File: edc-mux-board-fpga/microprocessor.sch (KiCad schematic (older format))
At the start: 27 parts

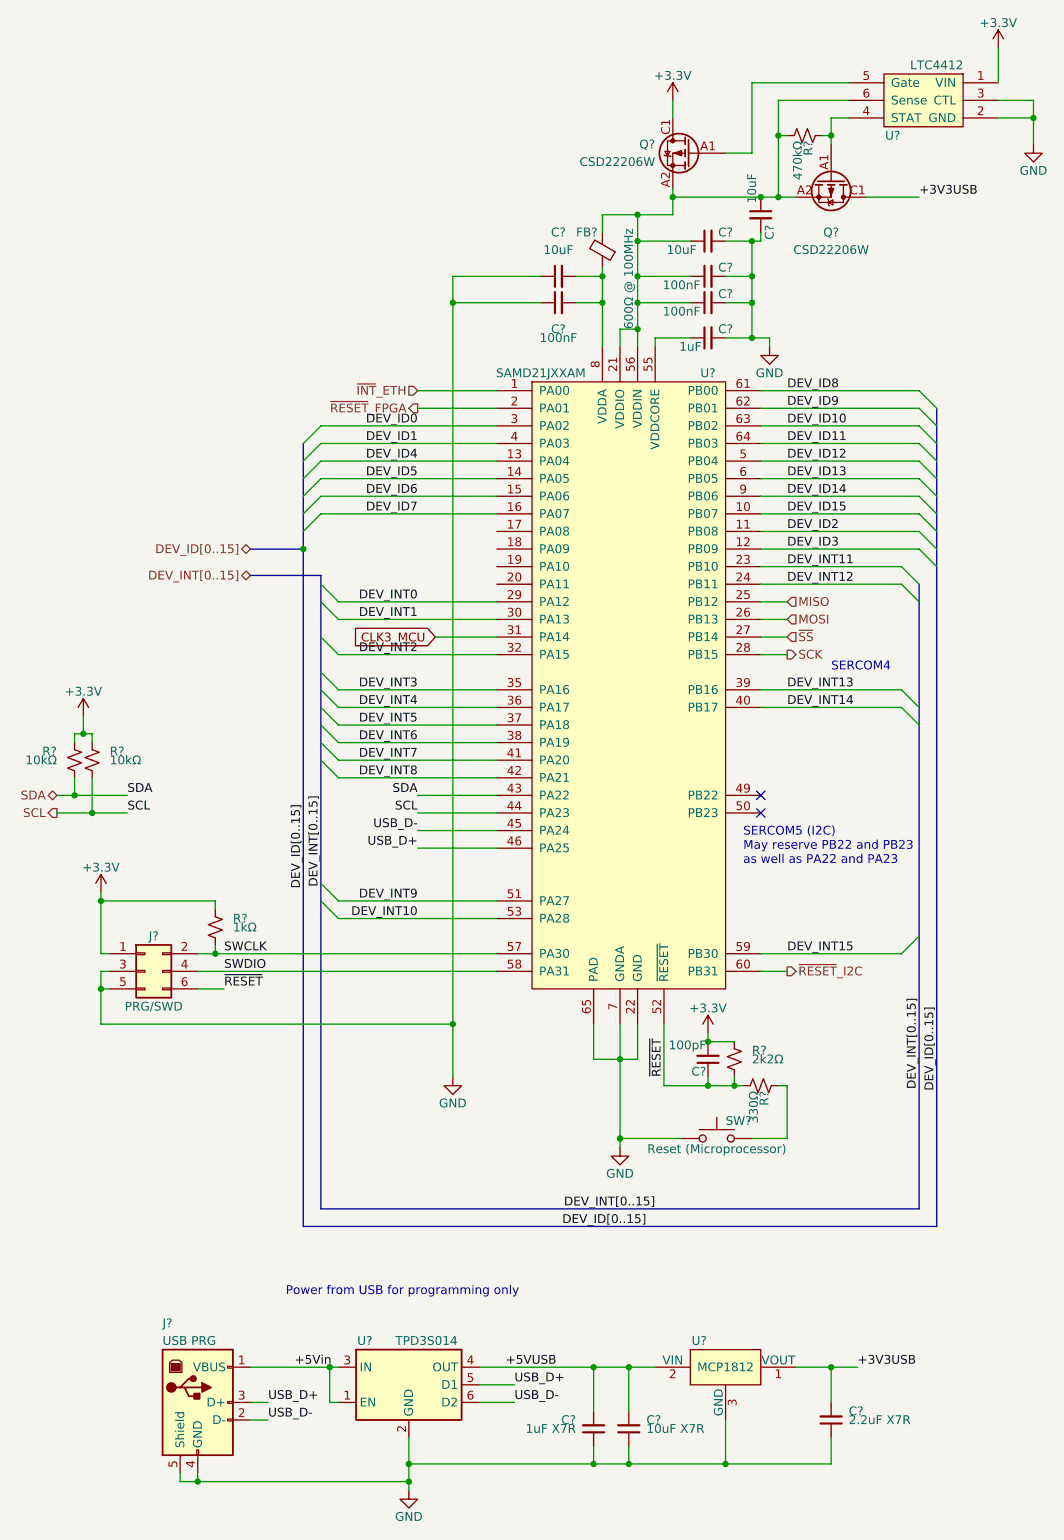
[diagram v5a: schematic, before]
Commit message: Finished FPGA and MCU interconnections.
Finished up interrupt wiring
Fixed a few missing connections
Annotated Schematic
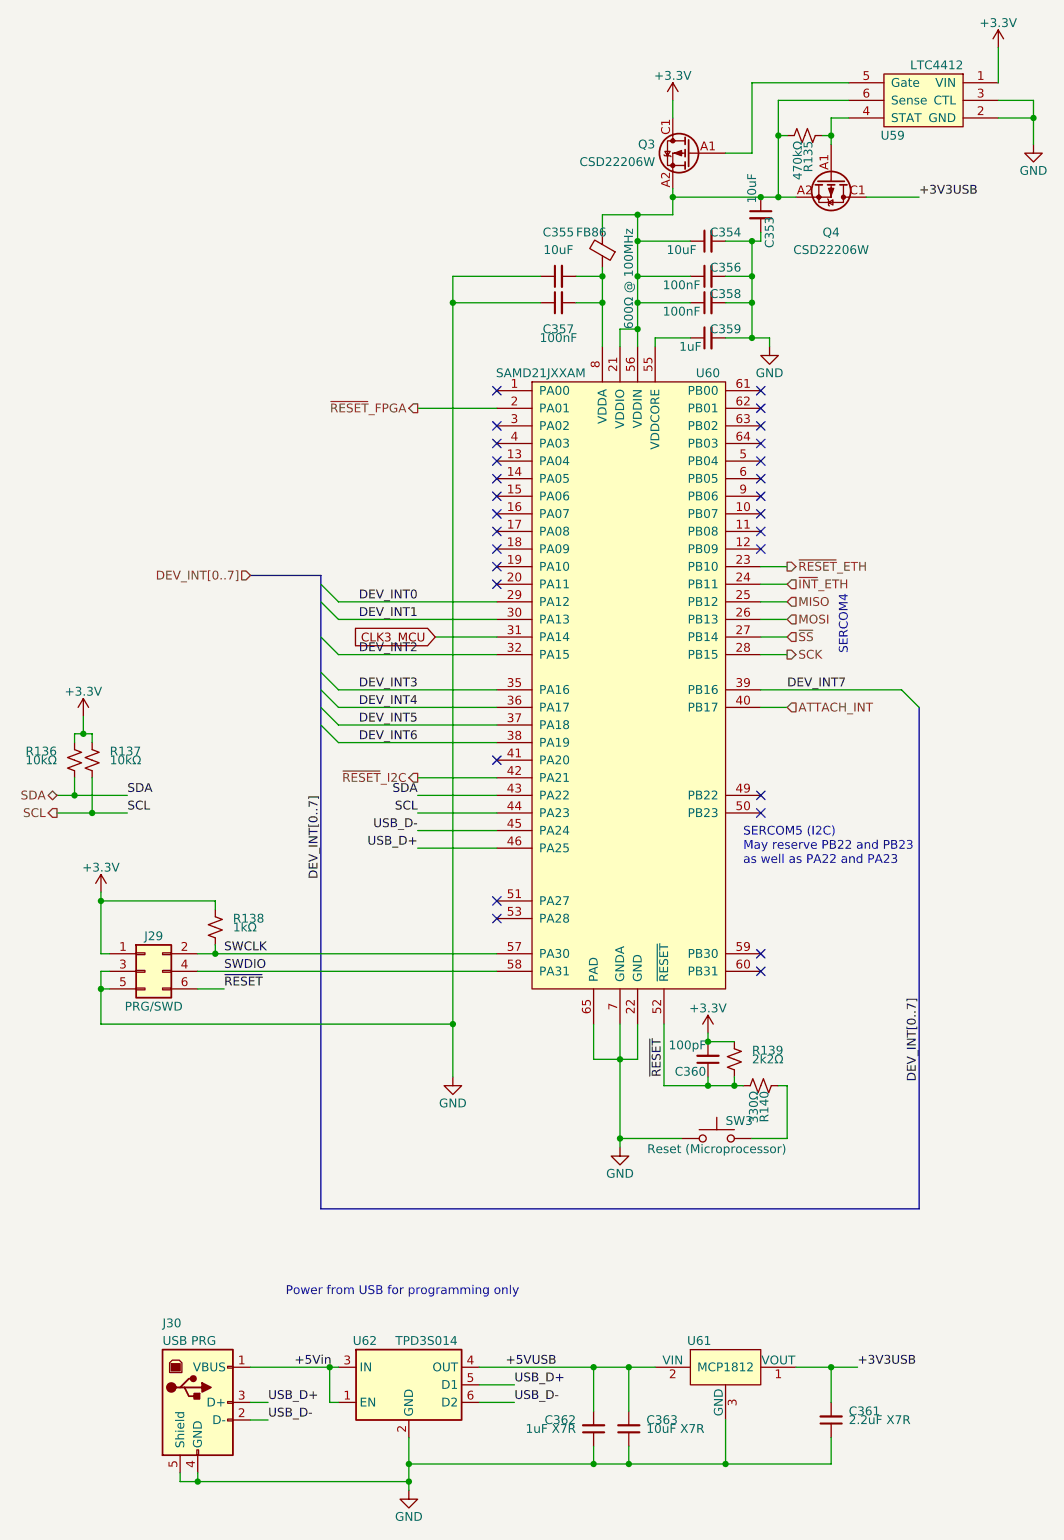
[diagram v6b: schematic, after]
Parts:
- gave numbers to parts that had none: 27
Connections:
- net DEV_INT12 is gone; now on net ~INT~_ETH: U60.24 (PB11)
- net DEV_INT13 is gone; now on net DEV_INT7: U60.39 (PB16)
- net DEV_INT8 is gone; now on net ~RESET~_I2C: U60.42 (PA21)
- net DEV_INT7: no longer U60.41 (PA20)
- net ~INT~_ETH: no longer U60.1 (PA00)
- net ~RESET~_I2C: no longer U60.60 (PB31)
- net DEV_ID0: no longer names the net of U60.3 (PA02)
- net DEV_ID1: no longer names the net of U60.4 (PA03)
- net DEV_ID10: no longer names the net of U60.63 (PB02)
- net DEV_ID11: no longer names the net of U60.64 (PB03)
- net DEV_ID12: no longer names the net of U60.5 (PB04)
- net DEV_ID13: no longer names the net of U60.6 (PB05)
- net DEV_ID14: no longer names the net of U60.9 (PB06)
- net DEV_ID15: no longer names the net of U60.10 (PB07)
- net DEV_ID2: no longer names the net of U60.11 (PB08)
- net DEV_ID3: no longer names the net of U60.12 (PB09)
- net DEV_ID4: no longer names the net of U60.13 (PA04)
- net DEV_ID5: no longer names the net of U60.14 (PA05)
- net DEV_ID6: no longer names the net of U60.15 (PA06)
- net DEV_ID7: no longer names the net of U60.16 (PA07)
- net DEV_ID8: no longer names the net of U60.61 (PB00)
- net DEV_ID9: no longer names the net of U60.62 (PB01)
- net DEV_INT10: no longer names the net of U60.53 (PA28)
- net DEV_INT11 renamed ~RESET~_ETH
- net DEV_INT14 renamed ATTACH_INT
- net DEV_INT15: no longer names the net of U60.59 (PB30)
- net DEV_INT9: no longer names the net of U60.51 (PA27)
- no-connect marks 2 -> 28

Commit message: assigned more footprints
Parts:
- C353, C354, C355: value 10uF -> 10uF X7R; footprint (none) -> Capacitor_SMD:C_1206_3216Metric; Manufacturer (none) -> Kemet; Manufacturers Part Number (none) -> C1206C106J3RACAUTO; Package ID (none) -> 1206in/3216mm
- C356, C357, C358, C360, C361: footprint (none) -> Capacitor_SMD:C_0603_1608Metric; Package ID (none) -> 0603in/1608mm
- C359: value 1uF -> 1uF X7R; footprint (none) -> Capacitor_SMD:C_0603_1608Metric; Manufacturer (none) -> TDK; Manufacturers Part Number (none) -> CGA3E1X7R1E105K080AC; Package ID (none) -> 0603in/1608mm
- C362: footprint (none) -> Capacitor_SMD:C_0603_1608Metric; Manufacturer (none) -> TDK; Manufacturers Part Number (none) -> CGA3E1X7R1E105K080AC; Package ID (none) -> 0603in/1608mm
- C363: footprint (none) -> Capacitor_SMD:C_1206_3216Metric; Manufacturer (none) -> Kemet; Manufacturers Part Number (none) -> C1206C106J3RACAUTO; Package ID (none) -> 1206in/3216mm
- J29: footprint (none) -> Connector_PinHeader_2.54mm:PinHeader_2x03_P2.54mm_Vertical
- J30: footprint (none) -> SW-CUI-INC:UJ2-BV-1-TH
- R135, R136, R137, R138, R139, R140: footprint (none) -> Resistor_SMD:R_0402_1005Metric
- U61: footprint (none) -> Package_TO_SOT_SMD:SOT-23; Description (none) -> 3v3 regulator 300mA; Manufacturer (none) -> Microchip; Manufacturers Part Number (none) -> MCP1812AT-033/TT
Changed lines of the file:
@@
 P 3900 2150
 F 0 "C355" V 4150 2150 50  0000 C CNN
-F 1 "10uF" V 4050 2150 50  0000 C CNN
-F 2 "" H 3900 2150 50  0001 C CNN
+F 1 "10uF X7R" V 4050 2150 50  0000 C CNN
+F 2 "Capacitor_SMD:C_1206_3216Metric" H 3900 2150 50  0001 C CNN
 F 3 "~" H 3900 2150 50  0001 C CNN
+F 4 "Kemet" H 0   0   50  0001 C CNN "Manufacturer"
+F 5 "C1206C106J3RACAUTO" H 0   0   50  0001 C CNN "Manufacturers Part Number"
+F 6 "1206in/3216mm" H 0   0   50  0001 C CNN "Package ID"
 	1    3900 2150
 	0    -1   -1   0
@@
 F 0 "C357" V 3750 2300 50  0000 C CNN
 F 1 "100nF" V 3700 2300 50  0000 C CNN
-F 2 "" H 3900 2300 50  0001 C CNN
+F 2 "Capacitor_SMD:C_0603_1608Metric" H 3900 2300 50  0001 C CNN
 F 3 "~" H 3900 2300 50  0001 C CNN
+F 4 "0603in/1608mm" H 0   0   50  0001 C CNN "Package ID"
 	1    3900 2300
 	0    -1   -1   0
@@
 F 0 "R140" H 5080 6770 50  0000 L CNN
 F 1 "330Ω" H 5080 6710 50  0000 L CNN
-F 2 "" H 5050 6750 50  0001 C CNN
+F 2 "Resistor_SMD:R_0402_1005Metric" H 5050 6750 50  0001 C CNN
 F 3 "~" H 5050 6750 50  0001 C CNN
 	1    5050 6750
@@
 F 0 "C360" H 4760 6670 50  0000 L CNN
 F 1 "100pF" H 4760 6520 50  0000 L CNN
-F 2 "" H 4750 6600 50  0001 C CNN
+F 2 "Capacitor_SMD:C_0603_1608Metric" H 4750 6600 50  0001 C CNN
 F 3 "~" H 4750 6600 50  0001 C CNN
+F 4 "0603in/1608mm" H 0   0   50  0001 C CNN "Package ID"
 	1    4750 6600
 	-1   0    0    1
@@
 F 0 "R139" H 4800 6550 50  0000 R CNN
 F 1 "2k2Ω" H 4800 6600 50  0000 R CNN
-F 2 "" H 4900 6600 50  0001 C CNN
+F 2 "Resistor_SMD:R_0402_1005Metric" H 4900 6600 50  0001 C CNN
 F 3 "~" H 4900 6600 50  0001 C CNN
 	1    4900 6600
@@
 P 4750 1950
 F 0 "C354" V 4800 1850 50  0000 C CNN
-F 1 "10uF" V 4700 2100 50  0000 C CNN
-F 2 "" H 4750 1950 50  0001 C CNN
+F 1 "10uF X7R" V 4700 2100 50  0000 C CNN
+F 2 "Capacitor_SMD:C_1206_3216Metric" H 4750 1950 50  0001 C CNN
 F 3 "~" H 4750 1950 50  0001 C CNN
+F 4 "Kemet" H 0   0   50  0001 C CNN "Manufacturer"
+F 5 "C1206C106J3RACAUTO" H 0   0   50  0001 C CNN "Manufacturers Part Number"
+F 6 "1206in/3216mm" H 0   0   50  0001 C CNN "Package ID"
 	1    4750 1950
 	0    -1   -1   0
@@
 F 0 "C356" V 4800 2050 50  0000 C CNN
 F 1 "100nF" V 4700 2300 50  0000 C CNN
-F 2 "" H 4750 2150 50  0001 C CNN
+F 2 "Capacitor_SMD:C_0603_1608Metric" H 4750 2150 50  0001 C CNN
 F 3 "~" H 4750 2150 50  0001 C CNN
+F 4 "0603in/1608mm" H 0   0   50  0001 C CNN "Package ID"
 	1    4750 2150
 	0    -1   -1   0
@@
 F 0 "C358" V 4800 2200 50  0000 C CNN
 F 1 "100nF" V 4700 2450 50  0000 C CNN
-F 2 "" H 4750 2300 50  0001 C CNN
+F 2 "Capacitor_SMD:C_0603_1608Metric" H 4750 2300 50  0001 C CNN
 F 3 "~" H 4750 2300 50  0001 C CNN
+F 4 "0603in/1608mm" H 0   0   50  0001 C CNN "Package ID"
 	1    4750 2300
 	0    -1   -1   0
@@
 P 4750 2500
 F 0 "C359" V 4800 2400 50  0000 C CNN
-F 1 "1uF" V 4700 2600 50  0000 C CNN
-F 2 "" H 4750 2500 50  0001 C CNN
+F 1 "1uF X7R" V 4700 2600 50  0000 C CNN
+F 2 "Capacitor_SMD:C_0603_1608Metric" H 4750 2500 50  0001 C CNN
 F 3 "~" H 4750 2500 50  0001 C CNN
+F 4 "TDK" H 0   0   50  0001 C CNN "Manufacturer"
+F 5 "CGA3E1X7R1E105K080AC" H 0   0   50  0001 C CNN "Manufacturers Part Number"
+F 6 "0603in/1608mm" H 0   0   50  0001 C CNN "Package ID"
 	1    4750 2500
 	0    -1   -1   0
@@
 F 0 "R138" H 1850 5800 50  0000 R CNN
 F 1 "1kΩ" H 1850 5850 50  0000 R CNN
-F 2 "" H 1950 5850 50  0001 C CNN
+F 2 "Resistor_SMD:R_0402_1005Metric" H 1950 5850 50  0001 C CNN
 F 3 "~" H 1950 5850 50  0001 C CNN
 	1    1950 5850
@@
 F 0 "J29" H 1600 6300 50  0000 C CNN
 F 1 "PRG/SWD" H 1600 5900 50  0000 C CNN
-F 2 "" H 1550 6100 50  0001 C CNN
+F 2 "Connector_PinHeader_2.54mm:PinHeader_2x03_P2.54mm_Vertical" H 1550 6100 50  0001 C CNN
 F 3 "~" H 1550 6100 50  0001 C CNN
 	1    1550 6100
@@
 F 0 "J30" H 1650 9000 50  0000 L CNN
 F 1 "USB PRG" H 1650 8900 50  0000 L CNN
-F 2 "" H 2000 8500 50  0001 C CNN
+F 2 "SW-CUI-INC:UJ2-BV-1-TH" H 2000 8500 50  0001 C CNN
 F 3 " ~" H 2000 8500 50  0001 C CNN
 	1    1850 8550
@@
 F 0 "U61" H 4700 8500 50  0000 C CNN
 F 1 "MCP1812" H 4850 8350 50  0000 C CNN
-F 2 "" H 4800 8600 50  0001 C CNN
+F 2 "Package_TO_SOT_SMD:SOT-23" H 4800 8600 50  0001 C CNN
 F 3 "http://ww1.microchip.com/downloads/en/DeviceDoc/MCP1811A-11B-12A-12B-Data-Sheet-20006088B.pdf" H 4800 8600 50  0001 C CNN
 F 4 "SOT-23/SC70/SOT-323" H 4900 8550 50  0001 C CNN "Package ID"
+F 5 "Microchip" H 4850 8350 50  0001 C CNN "Manufacturer"
+F 6 "3v3 regulator 300mA" H 4850 8350 50  0001 C CNN "Description"
+F 7 "MCP1812AT-033/TT" H 4850 8350 50  0001 C CNN "Manufacturers Part Number"
 	1    4850 8350
 	1    0    0    -1
@@
 F 0 "C362" H 4200 8650 50  0000 L CNN
 F 1 "1uF X7R" H 4200 8700 50  0000 L CNN
-F 2 "" H 4100 8700 50  0001 C CNN
+F 2 "Capacitor_SMD:C_0603_1608Metric" H 4100 8700 50  0001 C CNN
 F 3 "~" H 4100 8700 50  0001 C CNN
+F 4 "TDK" H 0   0   50  0001 C CNN "Manufacturer"
+F 5 "CGA3E1X7R1E105K080AC" H 0   0   50  0001 C CNN "Manufacturers Part Number"
+F 6 "0603in/1608mm" H 0   0   50  0001 C CNN "Package ID"
 	1    4100 8700
 	-1   0    0    1
@@
 F 0 "C361" H 5350 8600 50  0000 R CNN
 F 1 "2.2uF X7R" H 5350 8650 50  0000 R CNN
-F 2 "" H 5450 8650 50  0001 C CNN
+F 2 "Capacitor_SMD:C_0603_1608Metric" H 5450 8650 50  0001 C CNN
 F 3 "~" H 5450 8650 50  0001 C CNN
+F 4 "0603in/1608mm" H 0   0   50  0001 C CNN "Package ID"
 	1    5450 8650
 	-1   0    0    1
@@
 F 0 "C363" H 4200 8650 50  0000 R CNN
 F 1 "10uF X7R" H 4200 8700 50  0000 R CNN
-F 2 "" H 4300 8700 50  0001 C CNN
+F 2 "Capacitor_SMD:C_1206_3216Metric" H 4300 8700 50  0001 C CNN
 F 3 "~" H 4300 8700 50  0001 C CNN
+F 4 "Kemet" H 0   0   50  0001 C CNN "Manufacturer"
+F 5 "C1206C106J3RACAUTO" H 0   0   50  0001 C CNN "Manufacturers Part Number"
+F 6 "1206in/3216mm" H 0   0   50  0001 C CNN "Package ID"
 	1    4300 8700
 	-1   0    0    1
@@
 F 0 "R135" H 5330 1370 50  0000 L CNN
 F 1 "470kΩ" H 5330 1310 50  0000 L CNN
-F 2 "" H 5300 1350 50  0001 C CNN
+F 2 "Resistor_SMD:R_0402_1005Metric" H 5300 1350 50  0001 C CNN
 F 3 "~" H 5300 1350 50  0001 C CNN
 	1    5300 1350
@@
 P 5050 1800
 F 0 "C353" V 5100 1700 50  0000 C CNN
-F 1 "10uF" V 5000 1950 50  0000 C CNN
-F 2 "" H 5050 1800 50  0001 C CNN
+F 1 "10uF X7R" V 5000 1950 50  0000 C CNN
+F 2 "Capacitor_SMD:C_1206_3216Metric" H 5050 1800 50  0001 C CNN
 F 3 "~" H 5050 1800 50  0001 C CNN
+F 4 "Kemet" H 0   0   50  0001 C CNN "Manufacturer"
+F 5 "C1206C106J3RACAUTO" H 0   0   50  0001 C CNN "Manufacturers Part Number"
+F 6 "1206in/3216mm" H 0   0   50  0001 C CNN "Package ID"
 	1    5050 1800
 	1    0    0    -1
@@
 F 0 "R137" H 1150 4850 50  0000 R CNN
 F 1 "10kΩ" H 1150 4900 50  0000 R CNN
-F 2 "" H 1250 4900 50  0001 C CNN
+F 2 "Resistor_SMD:R_0402_1005Metric" H 1250 4900 50  0001 C CNN
 F 3 "~" H 1250 4900 50  0001 C CNN
 	1    1250 4900
@@
 F 0 "R136" H 1250 4850 50  0000 L CNN
 F 1 "10kΩ" H 1250 4900 50  0000 L CNN
-F 2 "" H 1150 4900 50  0001 C CNN
+F 2 "Resistor_SMD:R_0402_1005Metric" H 1150 4900 50  0001 C CNN
 F 3 "~" H 1150 4900 50  0001 C CNN
 	1    1150 4900

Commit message: fixed USB connector by using my own *sane* libraries
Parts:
- J30: symbol Connector:USB_B -> SW-con:USB_B
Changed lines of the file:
@@
 	1300 6200 1300 6400
 $Comp
-L Connector:USB_B J30
+L SW-con:USB_B J30
 U 1 1 5CB54E9E
 P 1850 8550
